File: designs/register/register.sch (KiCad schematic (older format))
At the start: 37 parts, among them J101 Conn_01x08, J102 Conn_01x02_Power, J103 Conn_01x08, J104 Conn_01x01, J105 Conn_01x01, J106 Conn_01x08, J107 Conn_01x08, J108 Conn_01x08, J109 Conn_01x01, Q101 2N7000, Q102 2N7000, Q103 BC547, Q104 2N7000, Q105 2N7000, Q106 2N7000, Q107 2N7000, Q108 2N7000, Q109 2N7000, Q110 2N7000, Q111 2N7000, Q112 2N7000, Q113 2N7000, Q114 2N7000, Q115 2N7000, Q116 2N7000, Q117 2N7000, Q118 2N7000, Q119 2N7000, Q120 2N7000, Q121 2N7000

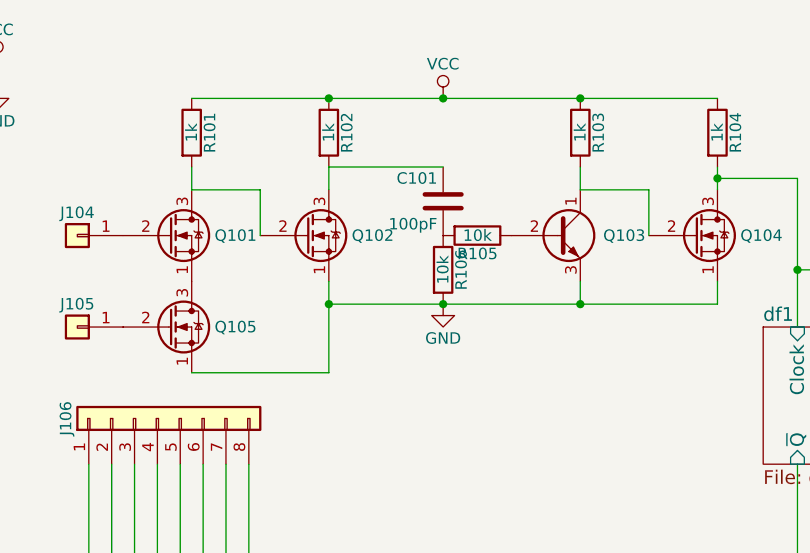
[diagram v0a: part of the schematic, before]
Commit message: Updated register design to fix small flaw.
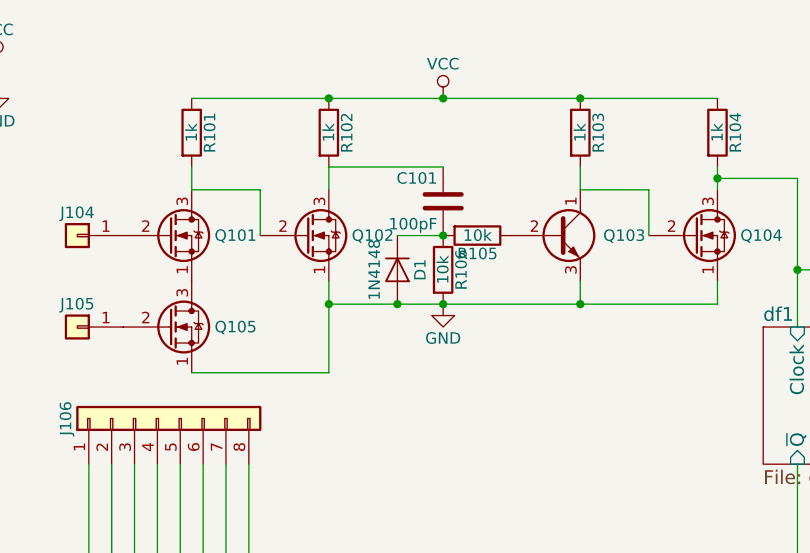
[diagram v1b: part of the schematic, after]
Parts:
- added D1: 1N4148, footprints:D_default, symbol 1N4148
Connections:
- net GND: now also D1.2 (A)
- net at C101.2, R105.2, R106.1: now also D1.1 (K)
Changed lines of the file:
@@
 $EndComp
 Connection ~ 2750 900
+$Comp
+L 1N4148 D1
+U 1 1 5A5F8122
+P 2550 1650
+F 0 "D1" H 2550 1750 50  0000 C CNN
+F 1 "1N4148" H 2550 1550 50  0000 C CNN
+F 2 "footprints:D_default" H 2550 1475 50  0001 C CNN
+F 3 "" H 2550 1650 50  0001 C CNN
+	1    2550 1650
+	0    1    1    0
+$EndComp
+Wire Wire Line
+	2550 1500 2750 1500
+Connection ~ 2750 1500
+Connection ~ 2550 1800
 $EndSCHEMATC
